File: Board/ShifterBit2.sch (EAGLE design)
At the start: 18 parts, among them J1 HIROSE_DM3CS-SF, U1 LV321SOT23-5, U2 LV321SOT23-5

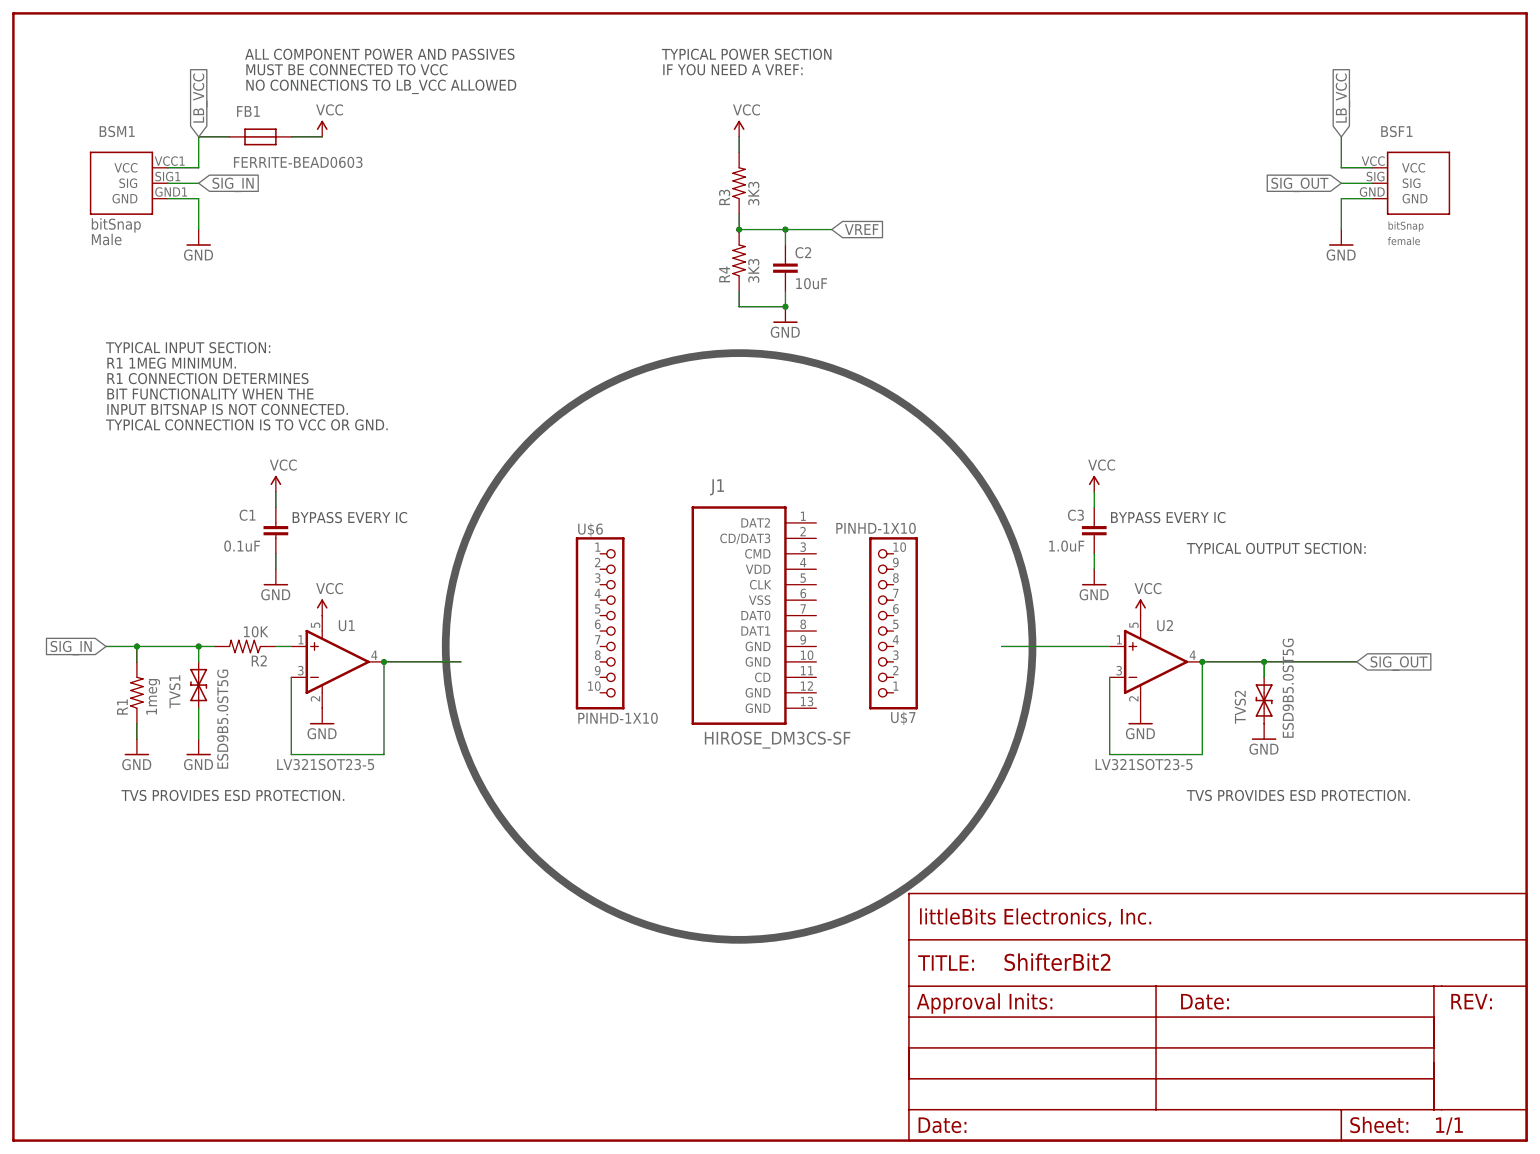
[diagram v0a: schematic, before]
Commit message: removed esd protection
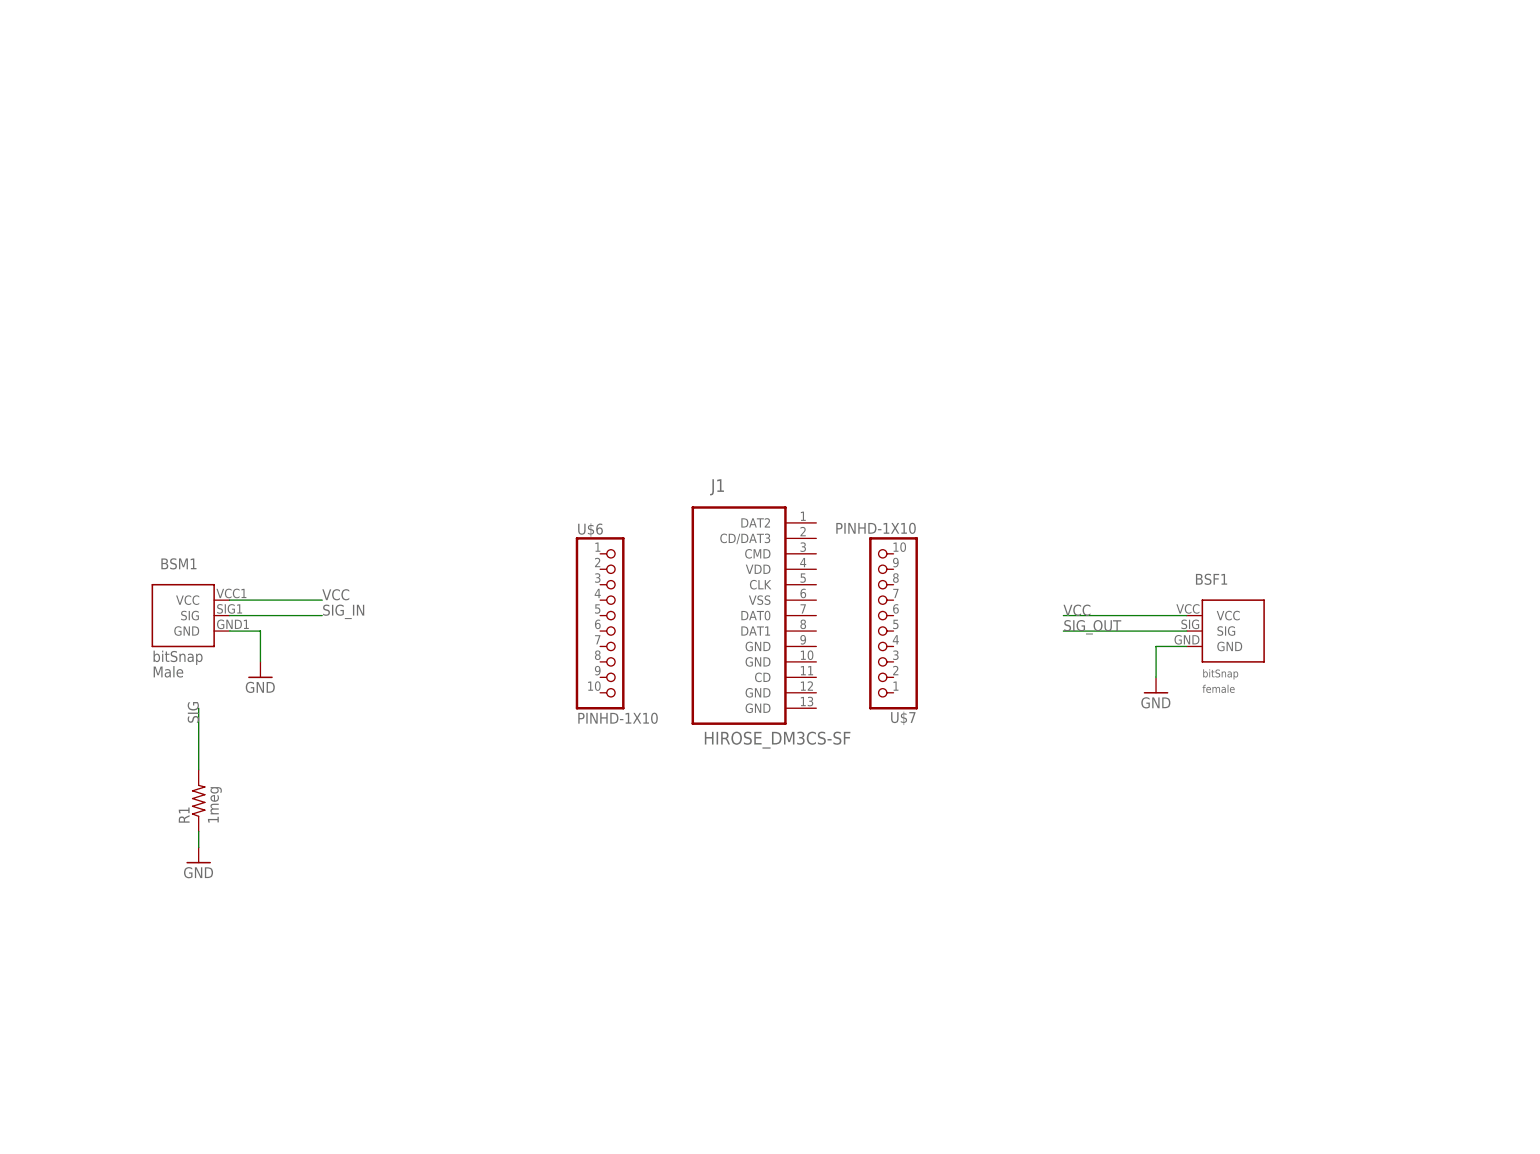
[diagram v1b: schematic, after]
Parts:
- removed C1: 0.1uF, LITTLEBITS:CAPCAP-0603
- removed C2: 10uF, LITTLEBITS:CAPCAP-0603
- removed C3: 1.0uF, LITTLEBITS:CAPCAP-0603
- removed FB1: FERRITE-BEAD0603, LITTLEBITS:FERRITE-BEAD0603
- removed R2: 10K, LITTLEBITS:RESISTOR0603
- removed R3, R4: 3K3, LITTLEBITS:RESISTOR0603
- removed TVS1, TVS2: ESD9B5.0ST5G, LITTLEBITS:DIODE-TVSSOD-923
- removed U$5: FRAME-LETTER-OHWOHW, LITTLEBITS:FRAME-LETTER-OHWOHW
- removed U1, U2: LV321SOT23-5, LITTLEBITS:LV321SOT23-5
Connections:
- removed net LB_VCC: BSF1.VCC, BSM1.VCC, FB1.P$2
- removed net N$2: U1.-IN, U1.OUT
- removed net N$3: U2.+IN
- removed net N$4: R2.1, U1.+IN
- removed net VREF: C2.1, R3.1, R4.2
- new net SIG: R1.2
- net GND: no longer C1.2, C2.2, C3.1, R4.1, TVS1.A, TVS2.A, U1.V-, U2.V-
- net SIG_IN: no longer R1.2, R2.2, TVS1.C
- net SIG_OUT: no longer TVS2.C, U2.-IN, U2.OUT
- net VCC: now also BSF1.VCC, BSM1.VCC; no longer C1.1, C3.2, FB1.P$1, R3.2, U1.V+, U2.V+
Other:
- note removed: "ALL COMPONENT POWER AND PASSIVES"
- note removed: "BIT FUNCTIONALITY WHEN THE"
- note removed: "BYPASS EVERY IC"
- note removed: "IF YOU NEED A VREF:"
- note removed: "INPUT BITSNAP IS NOT CONNECTED."
- note removed: "MUST BE CONNECTED TO VCC"
- note removed: "NO CONNECTIONS TO LB_VCC ALLOWED"
- note removed: "R1 1MEG MINIMUM."
- note removed: "R1 CONNECTION DETERMINES"
- note removed: "TVS PROVIDES ESD PROTECTION."
- note removed: "TYPICAL CONNECTION IS TO VCC OR GND."
- note removed: "TYPICAL INPUT SECTION:"
- note removed: "TYPICAL OUTPUT SECTION:"
- note removed: "TYPICAL POWER SECTION"
- moved on the sheet: BSF1, BSM1, R1

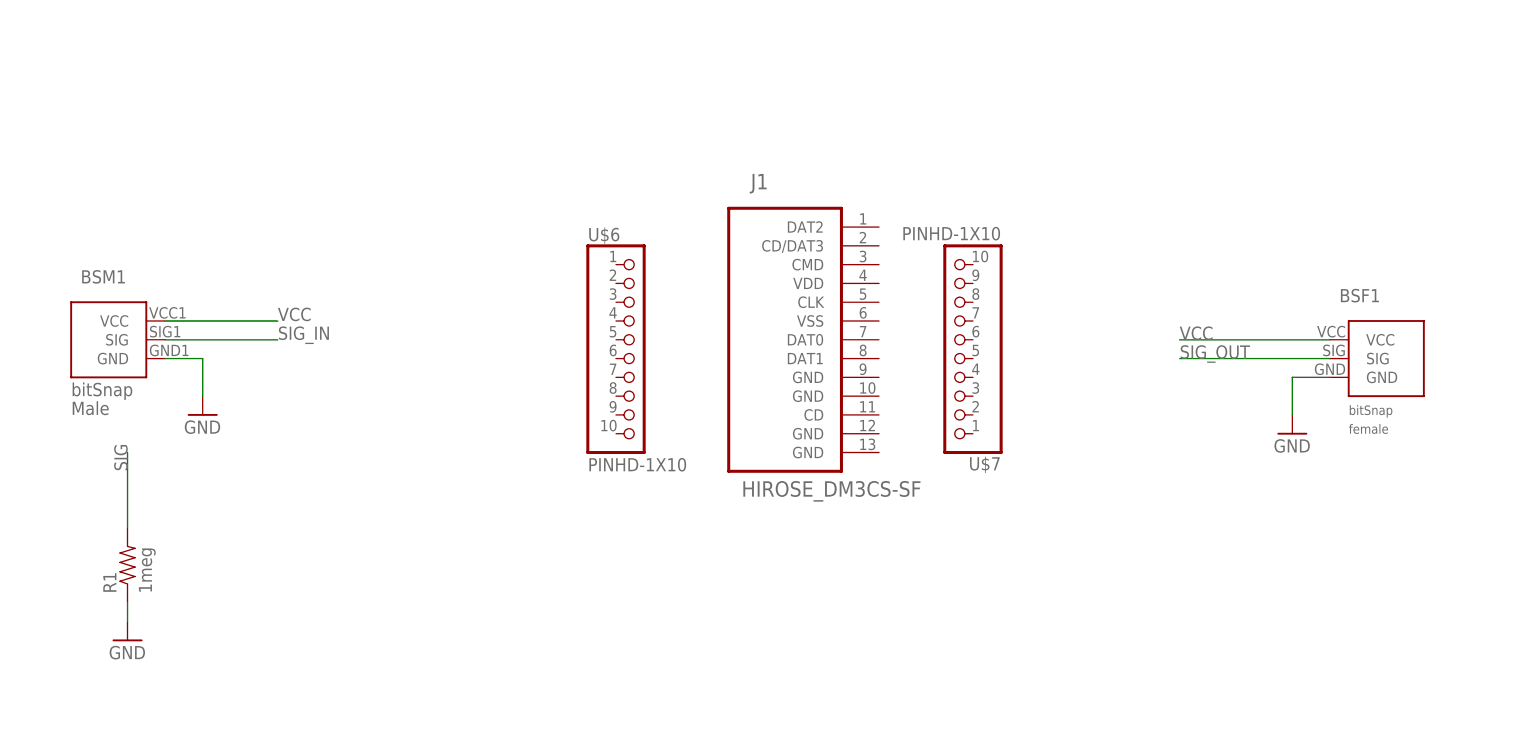
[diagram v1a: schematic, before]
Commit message: added nets and leds
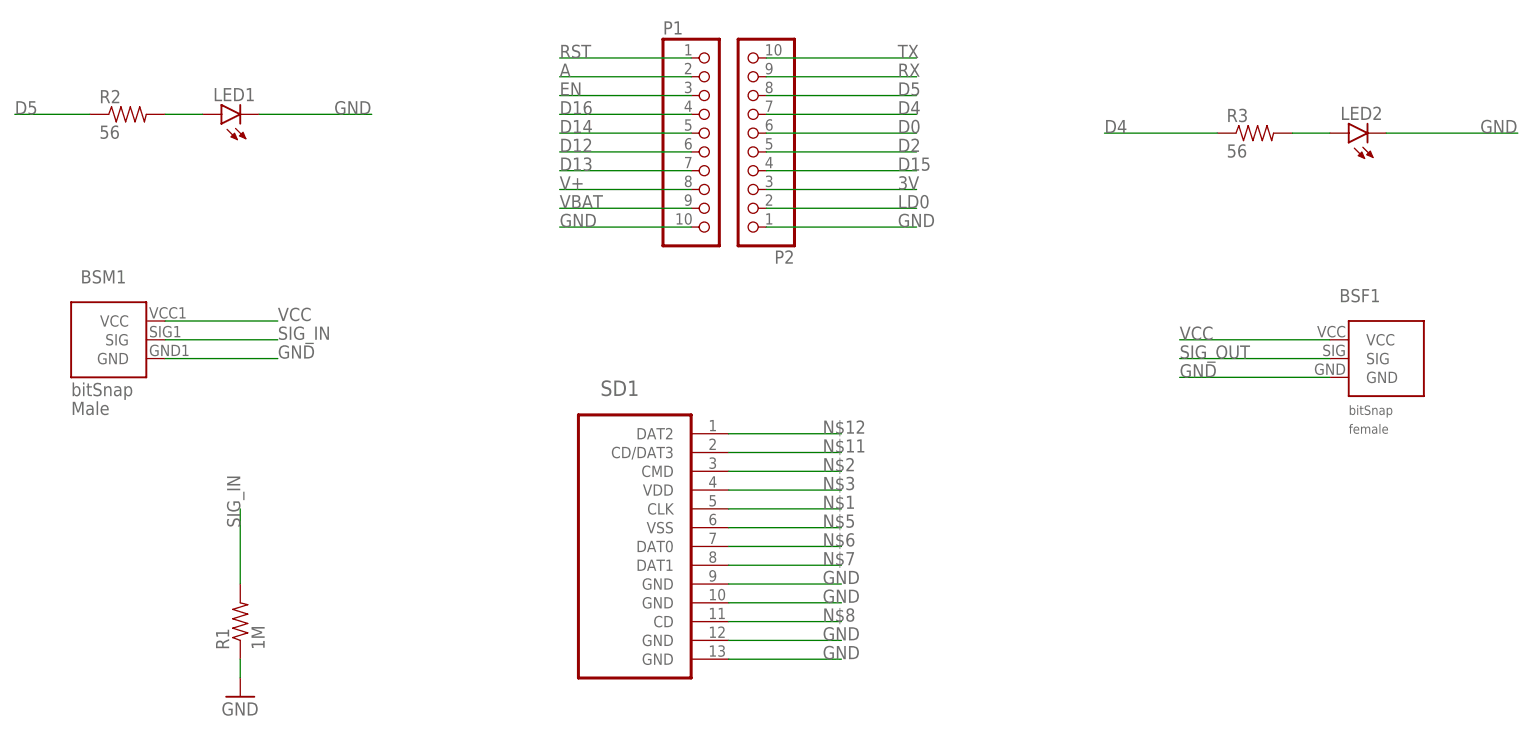
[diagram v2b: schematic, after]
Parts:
- removed J1: HIROSE_DM3CS-SF, HIROSE-DM3CS-SF:HIROSE_DM3CS-SF
- removed U$6, U$7: PINHD-1X10, adafruit:PINHD-1X10
- added LED1, LED2: (no value), SparkFun-LED:LED-GREEN0603
- added P1, P2: PINHD-1X10, adafruit:PINHD-1X10
- added R2, R3: 56, SparkFun-Passives:RESISTOR0603-RES
- added SD1: HIROSE_DM3CS-SF, HIROSE-DM3CS-SF:HIROSE_DM3CS-SF
- R1: value 1meg -> 1M
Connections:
- removed net SIG: R1.2
- new net 3V: P2.3
- new net A: P1.2
- new net D0: P2.6
- new net D12: P1.6
- new net D13: P1.7
- new net D14: P1.5
- new net D15: P2.4
- new net D16: P1.4
- new net D2: P2.5
- new net D4: P2.7, R3.1
- new net D5: P2.8, R2.1
- new net EN: P1.3
- new net LD0: P2.2
- new net N$1: SD1.CLK
- new net N$11: SD1.CD/DAT3
- new net N$12: SD1.DAT2
- new net N$2: SD1.CMD
- new net N$3: SD1.VDD
- new net N$4: LED1.A, R2.2
- new net N$5: SD1.VSS
- new net N$6: SD1.DAT0
- new net N$7: SD1.DAT1
- new net N$8: SD1.CD
- new net N$9: LED2.A, R3.2
- new net RST: P1.1
- new net RX: P2.9
- new net TX: P2.10
- new net V+: P1.8
- new net VBAT: P1.9
- net GND: now also LED1.C, LED2.C, P1.10, P2.1, SD1.GND@1, SD1.GND@2, SD1.GND@3, SD1.GND@4
- net SIG_IN: now also R1.2
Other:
- moved on the sheet: R1
